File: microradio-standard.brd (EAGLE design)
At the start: 96.5 x 64.4 mm, 13 parts, among them T1 NPN (ECB)

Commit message: added lib
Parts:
- C1, C2, C5: device capacitor-wima:C5B3 -> microradio-standard:C5B3
- C3: device rcl:B45181C -> microradio-standard:B45181A
- C4: device c-trimm:3008 -> microradio-standard:3008
- JP1, JP2: device pinhead:1X02 -> microradio-standard:1X02
- JP3: device pinhead:1X01 -> microradio-standard:1X01
- L1: device rcl:0204/5 -> microradio-standard:0204/5
- R1, R2, R3: device resistor:0204/7 -> microradio-standard:0207/7
- T1: device transistor:TO92 -> microradio-standard:TO92-BCE
- moved JP2 17.3 mm to (6.35, 31.8), turned to 0 degrees
- moved C3 16.5 mm to (16.5, 17.8)
- moved C5 16.5 mm to (45.7, 29.2)
- moved L1 16.5 mm to (34.3, 25.4)
- moved C1 16.5 mm to (31.8, 6.35)
- moved C2 16.5 mm to (45.7, 10.2)
- moved C4 16.5 mm to (50.8, 19.1)
- moved JP3 16.5 mm to (50.8, 7.62)
- moved R1 16.5 mm to (38.1, 6.35)
- moved R2 16.5 mm to (25.4, 6.35)
- moved R3 16.5 mm to (25.4, 27.9)
- moved T1 15.9 mm to (38.1, 19.1), turned to 270 degrees
- moved JP1 14.9 mm to (6.35, 17.8), turned to 180 degrees
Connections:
- net N$2: now also T1.E; no longer T1.1
- net N$4: now also T1.B; no longer T1.2
- net N$5: now also T1.C; no longer T1.3
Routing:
- net N$2: track 41.3 -> 20.1 mm
- net GND: track 119.9 -> 109.7 mm
- net N$5: track 25.2 -> 32.0 mm
- net N$4: track 40.5 -> 43.7 mm
- net N$3: track 44.5 -> 41.9 mm
- net N$1: track 6.35 -> 7.62 mm
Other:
- board size 96.5 x 64.4 mm -> 57.1 x 36.5 mm

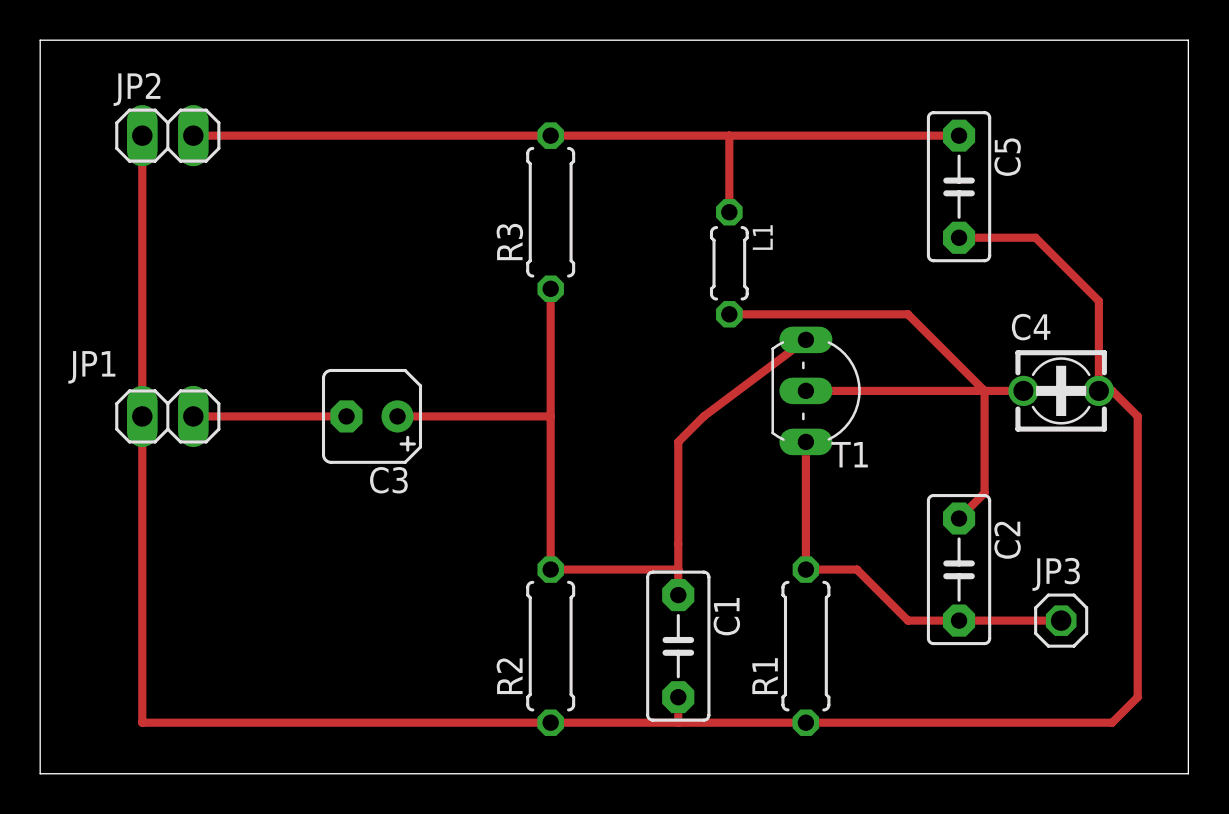
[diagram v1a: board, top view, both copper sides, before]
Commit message: moving to smd
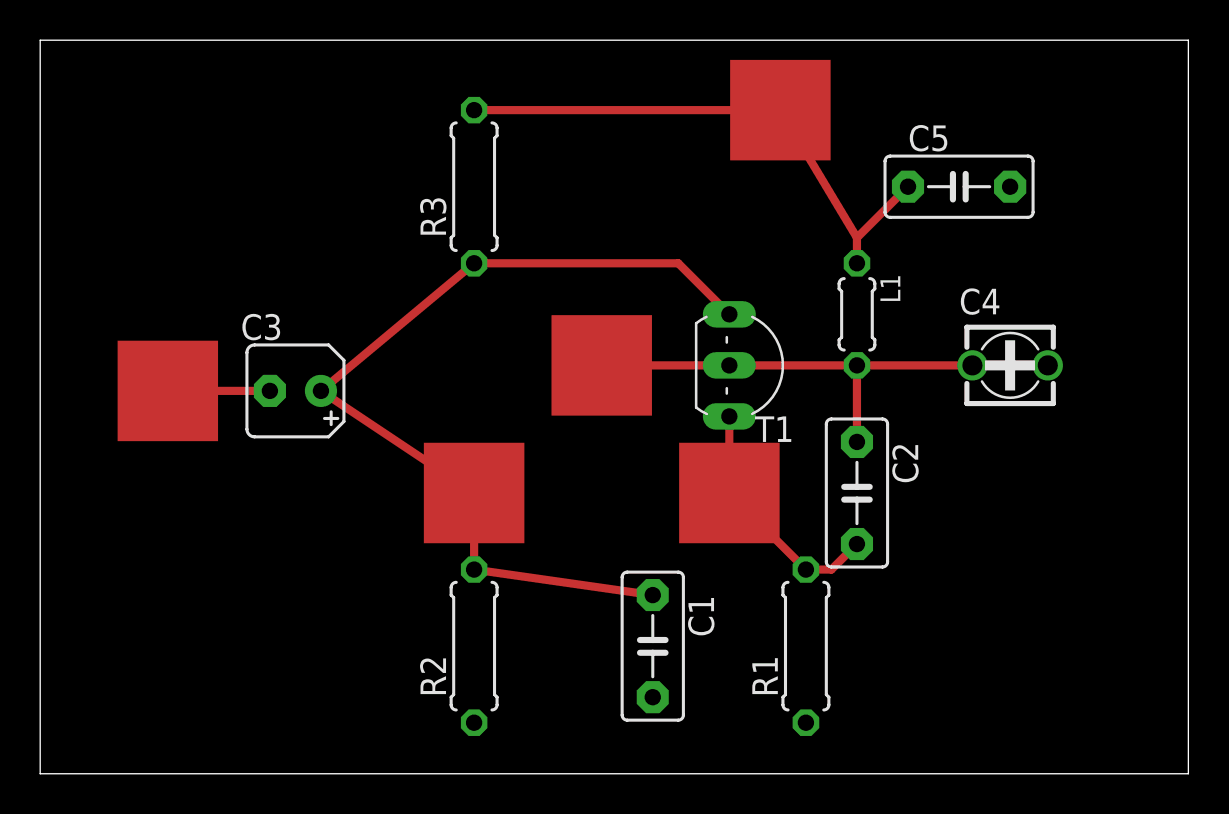
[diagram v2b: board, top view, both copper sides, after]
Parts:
- removed JP1: audio_in, microradio-standard:1X02
- removed JP2: BATT, microradio-standard:1X02
- removed JP3: RF, microradio-standard:1X01
- added MP1, MP2, MP3, MP4, MP5: MICROSTRIPMI, microradio-standard:MICROSTRIP_5X5MM
- C4: value 10pF -> 10-20pF
- moved L1 6.84 mm to (40.6, 22.9)
- moved C2 6.35 mm to (40.6, 14.0)
- moved C3 4.02 mm to (12.7, 19.1)
- moved T1 4.02 mm to (34.3, 20.3)
- moved R3 4.02 mm to (21.6, 29.2)
- moved R2 3.81 mm to (21.6, 6.35)
- moved C4 2.84 mm to (48.3, 20.3)
- moved C1 1.27 mm to (30.5, 6.35)
- turned C5 to 0 degrees
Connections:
- removed net N$5: C2.1, C4.+, L1.2, T1.C
- new net N$6: C2.1, C4.+, L1.2, MP4.F, T1.C
- net GND: no longer JP1.2, JP2.1
- net N$1: now also MP1.F; no longer JP1.1
- net N$2: now also MP5.F; no longer JP3.1
- net N$3: now also MP3.F; no longer JP2.2
- net N$4: now also MP2.F
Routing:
- net GND: track 109.7 -> 0.00 mm
- net N$5: track 32.0 -> 0.00 mm
- net N$6: track 0.00 -> 22.3 mm
- net N$3: track 41.9 -> 27.5 mm
- net N$2: track 20.1 -> 12.3 mm
- net N$1: track 7.62 -> 5.08 mm
- net N$4: track 43.7 -> 45.6 mm

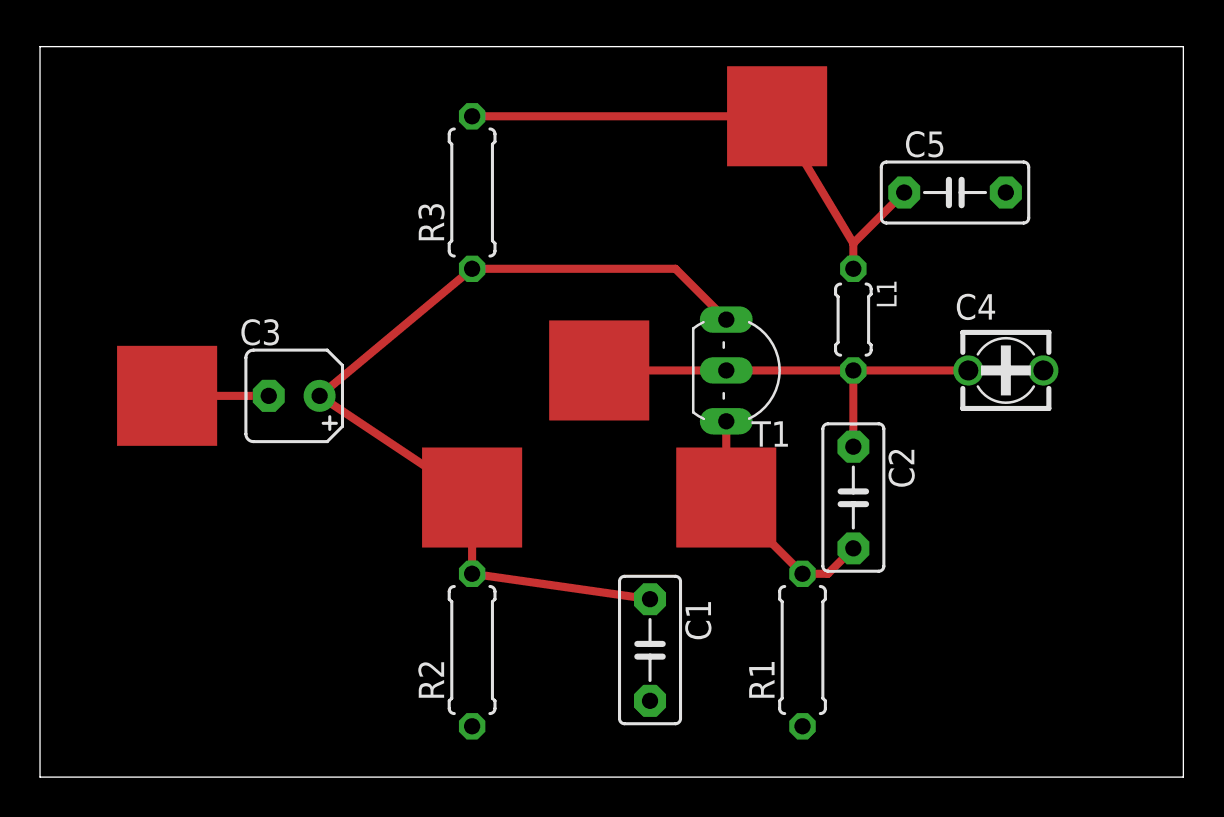
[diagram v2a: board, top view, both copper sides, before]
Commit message: smd version, is this legfit microstrip?
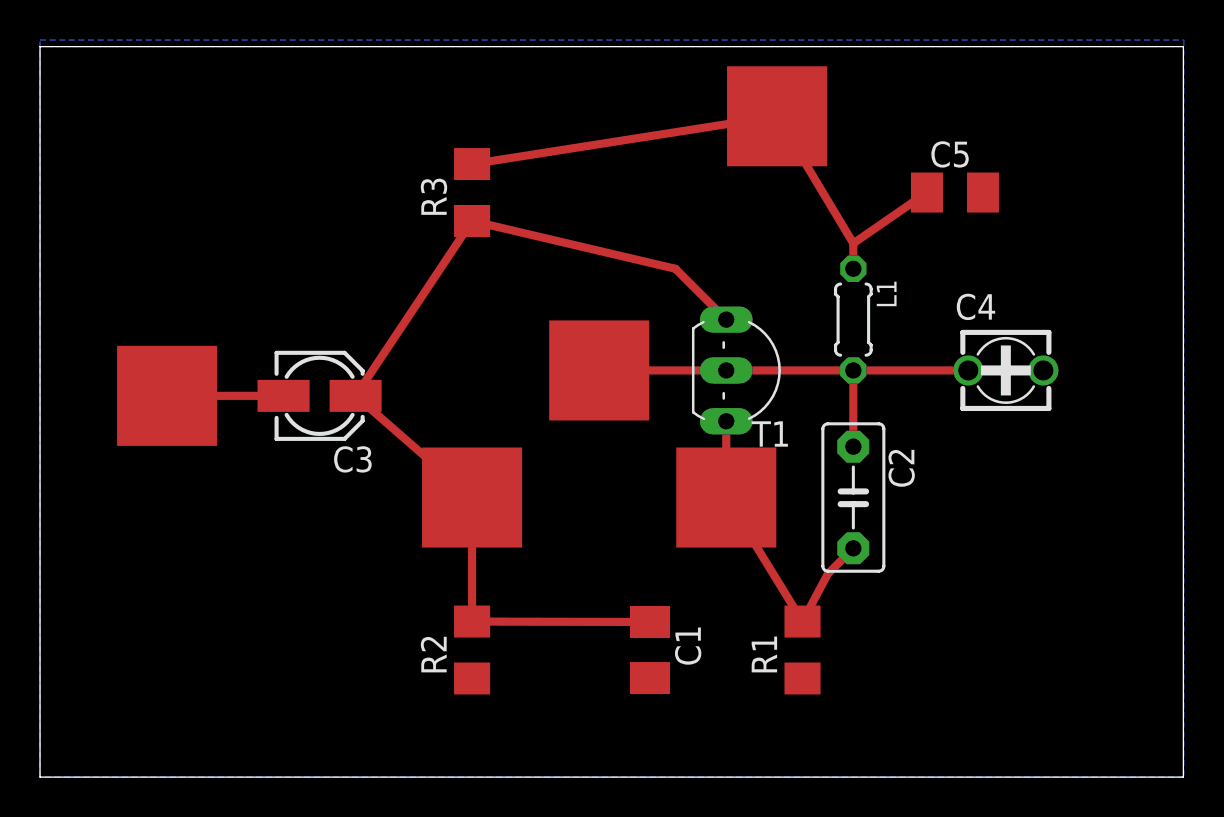
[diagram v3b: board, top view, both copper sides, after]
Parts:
- C1, C5: device microradio-standard:C5B3 -> microradio-standard:M1206
- C3: device microradio-standard:B45181A -> microradio-standard:153CLV-0405
- R1, R2, R3: device microradio-standard:0207/7 -> microradio-standard:R1206
- moved C3 1.27 mm to (14.0, 19.1), turned to 0 degrees
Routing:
- net N$2: track 12.3 -> 15.6 mm
- net N$4: track 45.6 -> 47.3 mm
- net N$3: track 27.5 -> 28.6 mm
- net N$1: track 5.08 -> 5.82 mm
- added copper zone on layer 16, net GND
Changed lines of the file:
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@@
 </autorouter>
 <elements>
-<element name="C1" library="microradio-standard" package="C5B3" value="0.01uF" x="30.48" y="6.35" rot="R270"/>
+<element name="C1" library="microradio-standard" package="M1206" value="0.01uF" x="30.48" y="6.35" rot="R270"/>
 <element name="C2" library="microradio-standard" package="C5B3" value="10pF" x="40.64" y="13.97" rot="R270"/>
 <element name="L1" library="microradio-standard" package="0204/5" value="" x="40.64" y="22.86" rot="R270"/>
-<element name="R1" library="microradio-standard" package="0207/7" value="470" x="38.1" y="6.35" rot="R90"/>
-<element name="R2" library="microradio-standard" package="0207/7" value="10K" x="21.59" y="6.35" rot="R90"/>
-<element name="R3" library="microradio-standard" package="0207/7" value="27K" x="21.59" y="29.21" rot="R90"/>
-<element name="C3" library="microradio-standard" package="B45181A" value="33uF" x="12.7" y="19.05" smashed="yes" rot="R180">
-<attribute name="NAME" x="12.065" y="22.86" size="1.27" layer="25" ratio="10" rot="R180"/>
-<attribute name="VALUE" x="16.002" y="15.621" size="1.27" layer="27" ratio="10" rot="R180"/>
+<element name="R1" library="microradio-standard" package="R1206" value="470" x="38.1" y="6.35" rot="R90"/>
+<element name="R2" library="microradio-standard" package="R1206" value="10K" x="21.59" y="6.35" rot="R90"/>
+<element name="R3" library="microradio-standard" package="R1206" value="27K" x="21.59" y="29.21" rot="R90"/>
+<element name="C3" library="microradio-standard" package="153CLV-0405" value="33uF" x="13.97" y="19.05" smashed="yes">
+<attribute name="NAME" x="14.605" y="15.24" size="1.27" layer="25" ratio="10"/>
+<attribute name="VALUE" x="10.668" y="22.479" size="1.27" layer="27" ratio="10"/>
 </element>
 <element name="C4" library="microradio-standard" package="3008" value="10-20pF" x="48.26" y="20.32">
@@
 <attribute name="VALUE" x="31.115" y="23.495" size="1.016" layer="27" ratio="10" rot="R270"/>
 </element>
-<element name="C5" library="microradio-standard" package="C5B3" value="0.01uF" x="45.72" y="29.21"/>
+<element name="C5" library="microradio-standard" package="M1206" value="0.01uF" x="45.72" y="29.21"/>
 <element name="MP2" library="microradio-standard" package="MICROSTRIP_5X5MM" value="MICROSTRIPMI" x="21.59" y="13.97"/>
 <element name="MP4" library="microradio-standard" package="MICROSTRIP_5X5MM" value="MICROSTRIPMI" x="27.94" y="20.32"/>
@@
 <contactref element="C3" pad="-"/>
 <contactref element="MP1" pad="F"/>
-<wire x1="11.43" y1="19.05" x2="6.35" y2="19.05" width="0.4064" layer="1"/>
+<wire x1="12.17" y1="19.05" x2="6.35" y2="19.05" width="0.4064" layer="1"/>
 </signal>
 <signal name="GND">
@@
 <contactref element="C4" pad="-"/>
 <contactref element="C1" pad="2"/>
-<wire x1="50.135" y1="20.32" x2="48.26" y2="29.21" width="0" layer="19" extent="1-1"/>
-<wire x1="38.1" y1="2.54" x2="50.135" y2="20.32" width="0" layer="19" extent="1-1"/>
-<wire x1="30.48" y1="3.81" x2="38.1" y2="2.54" width="0" layer="19" extent="1-1"/>
-<wire x1="21.59" y1="2.54" x2="30.48" y2="3.81" width="0" layer="19" extent="1-1"/>
+<polygon width="0.4064" layer="16">
+<vertex x="0" y="36.83"/>
+<vertex x="57.15" y="36.83"/>
+<vertex x="57.15" y="0"/>
+<vertex x="0" y="0"/>
+</polygon>
+<wire x1="50.135" y1="20.32" x2="47.12" y2="29.21" width="0" layer="19" extent="1-1"/>
+<wire x1="38.1" y1="4.928" x2="50.135" y2="20.32" width="0" layer="19" extent="1-1"/>
+<wire x1="30.48" y1="4.95" x2="38.1" y2="4.928" width="0" layer="19" extent="1-1"/>
+<wire x1="21.59" y1="4.928" x2="30.48" y2="4.95" width="0" layer="19" extent="1-1"/>
 </signal>
 <signal name="N$3">
@@
 <contactref element="MP3" pad="F"/>
 <wire x1="40.64" y1="26.67" x2="40.64" y2="25.4" width="0.4064" layer="1"/>
-<wire x1="40.64" y1="26.67" x2="43.18" y2="29.21" width="0.4064" layer="1"/>
-<wire x1="21.59" y1="33.02" x2="36.83" y2="33.02" width="0.4064" layer="1"/>
+<wire x1="40.64" y1="26.67" x2="44.32" y2="29.21" width="0.4064" layer="1"/>
+<wire x1="21.59" y1="30.632" x2="36.83" y2="33.02" width="0.4064" layer="1"/>
 <wire x1="36.83" y1="33.02" x2="40.64" y2="26.67" width="0.4064" layer="1"/>
 </signal>
@@
 <contactref element="C1" pad="1"/>
 <contactref element="MP2" pad="F"/>
-<wire x1="21.59" y1="13.97" x2="13.97" y2="19.05" width="0.4064" layer="1"/>
-<wire x1="21.59" y1="25.4" x2="13.97" y2="19.05" width="0.4064" layer="1"/>
+<wire x1="21.59" y1="13.97" x2="15.77" y2="19.05" width="0.4064" layer="1"/>
+<wire x1="21.59" y1="27.788" x2="15.77" y2="19.05" width="0.4064" layer="1"/>
 <wire x1="34.29" y1="22.86" x2="31.75" y2="25.4" width="0.4064" layer="1"/>
-<wire x1="31.75" y1="25.4" x2="21.59" y2="25.4" width="0.4064" layer="1"/>
-<wire x1="30.48" y1="8.89" x2="21.59" y2="10.16" width="0.4064" layer="1"/>
-<wire x1="21.59" y1="10.16" x2="21.59" y2="13.97" width="0.4064" layer="1"/>
+<wire x1="31.75" y1="25.4" x2="21.59" y2="27.788" width="0.4064" layer="1"/>
+<wire x1="30.48" y1="7.75" x2="21.59" y2="7.772" width="0.4064" layer="1"/>
+<wire x1="21.59" y1="7.772" x2="21.59" y2="13.97" width="0.4064" layer="1"/>
 </signal>
 <signal name="N$2">
@@
 <contactref element="C2" pad="2"/>
 <contactref element="MP5" pad="F"/>
-<wire x1="34.29" y1="13.97" x2="38.1" y2="10.16" width="0.4064" layer="1"/>
-<wire x1="38.1" y1="10.16" x2="39.37" y2="10.16" width="0.4064" layer="1"/>
+<wire x1="34.29" y1="13.97" x2="38.1" y2="7.772" width="0.4064" layer="1"/>
+<wire x1="38.1" y1="7.772" x2="39.37" y2="10.16" width="0.4064" layer="1"/>
 <wire x1="39.37" y1="10.16" x2="40.64" y2="11.43" width="0.4064" layer="1"/>
 <wire x1="34.29" y1="17.78" x2="34.29" y2="13.97" width="0.4064" layer="1"/>
